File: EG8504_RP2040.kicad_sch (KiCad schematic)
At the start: 52 parts, among them J1 USB_C_Receptacle_USB2.0_16P, J2 522712079, J3 Conn_01x03_Socket, J4 Conn_01x14_Socket, J5 Conn_01x14_Socket, SW1 SW_Push, SW2 SW_Push, U1 RP2040, U2 W25Q16JVSS, U3 MIC5504-3.3YM5, U4 USBLC6-2SC6, U5 MC34063AD, Y1 ECS-3225MV-xxx-xx

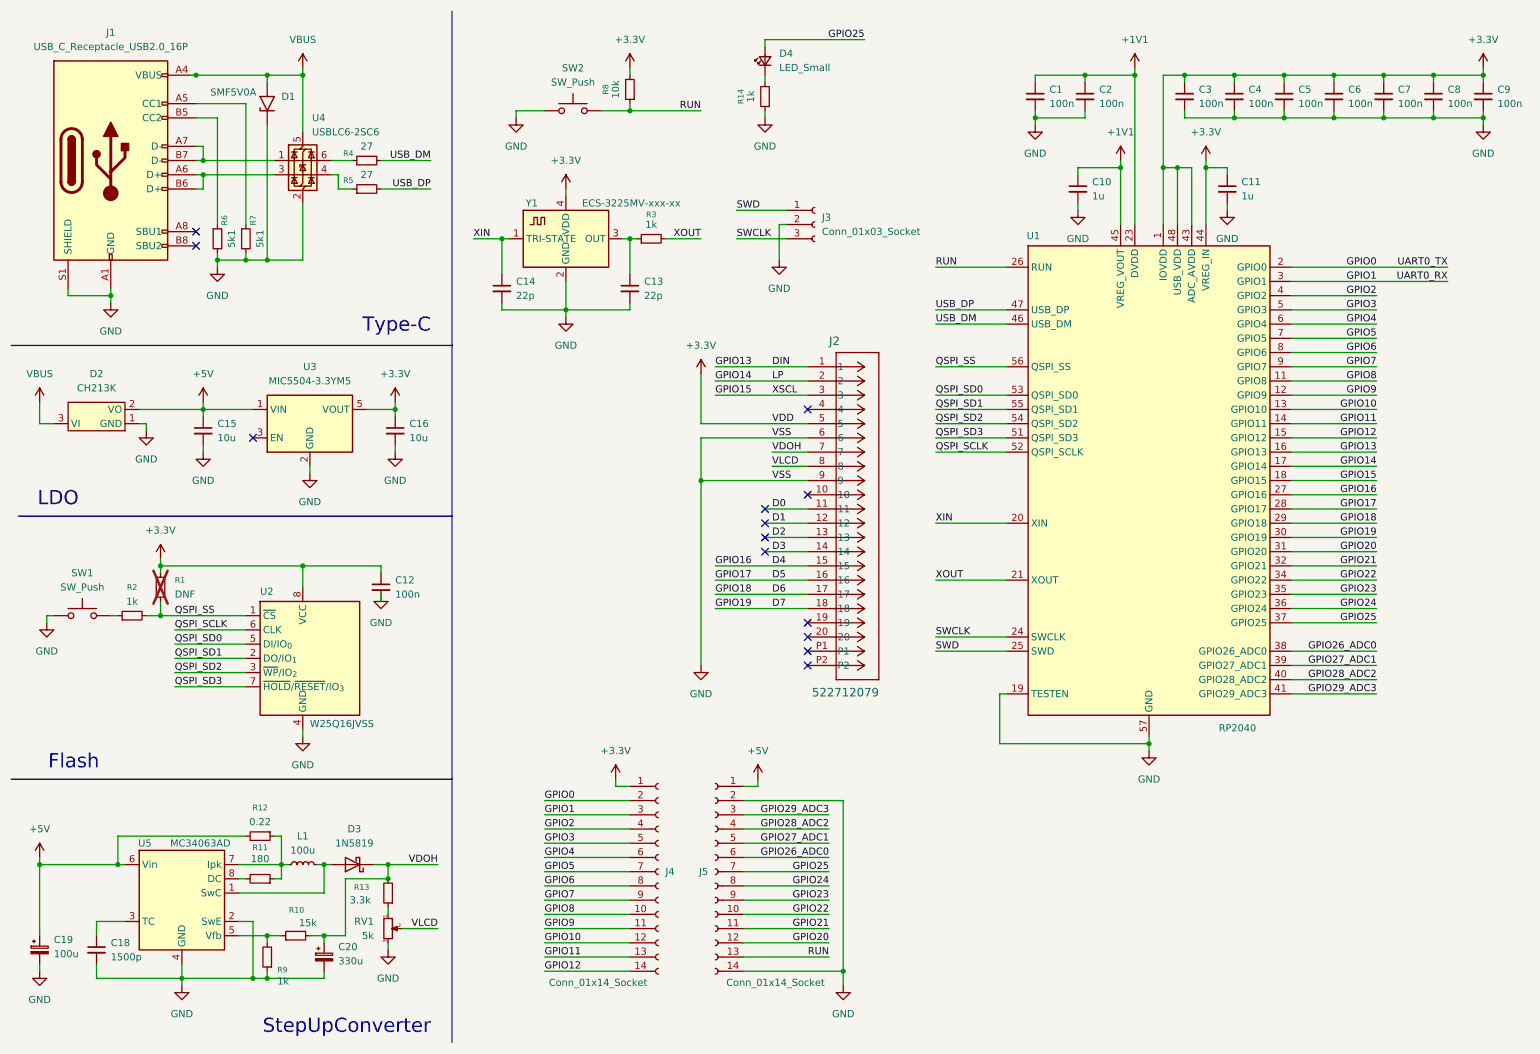
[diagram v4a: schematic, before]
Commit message: rp2040からpicoに変更
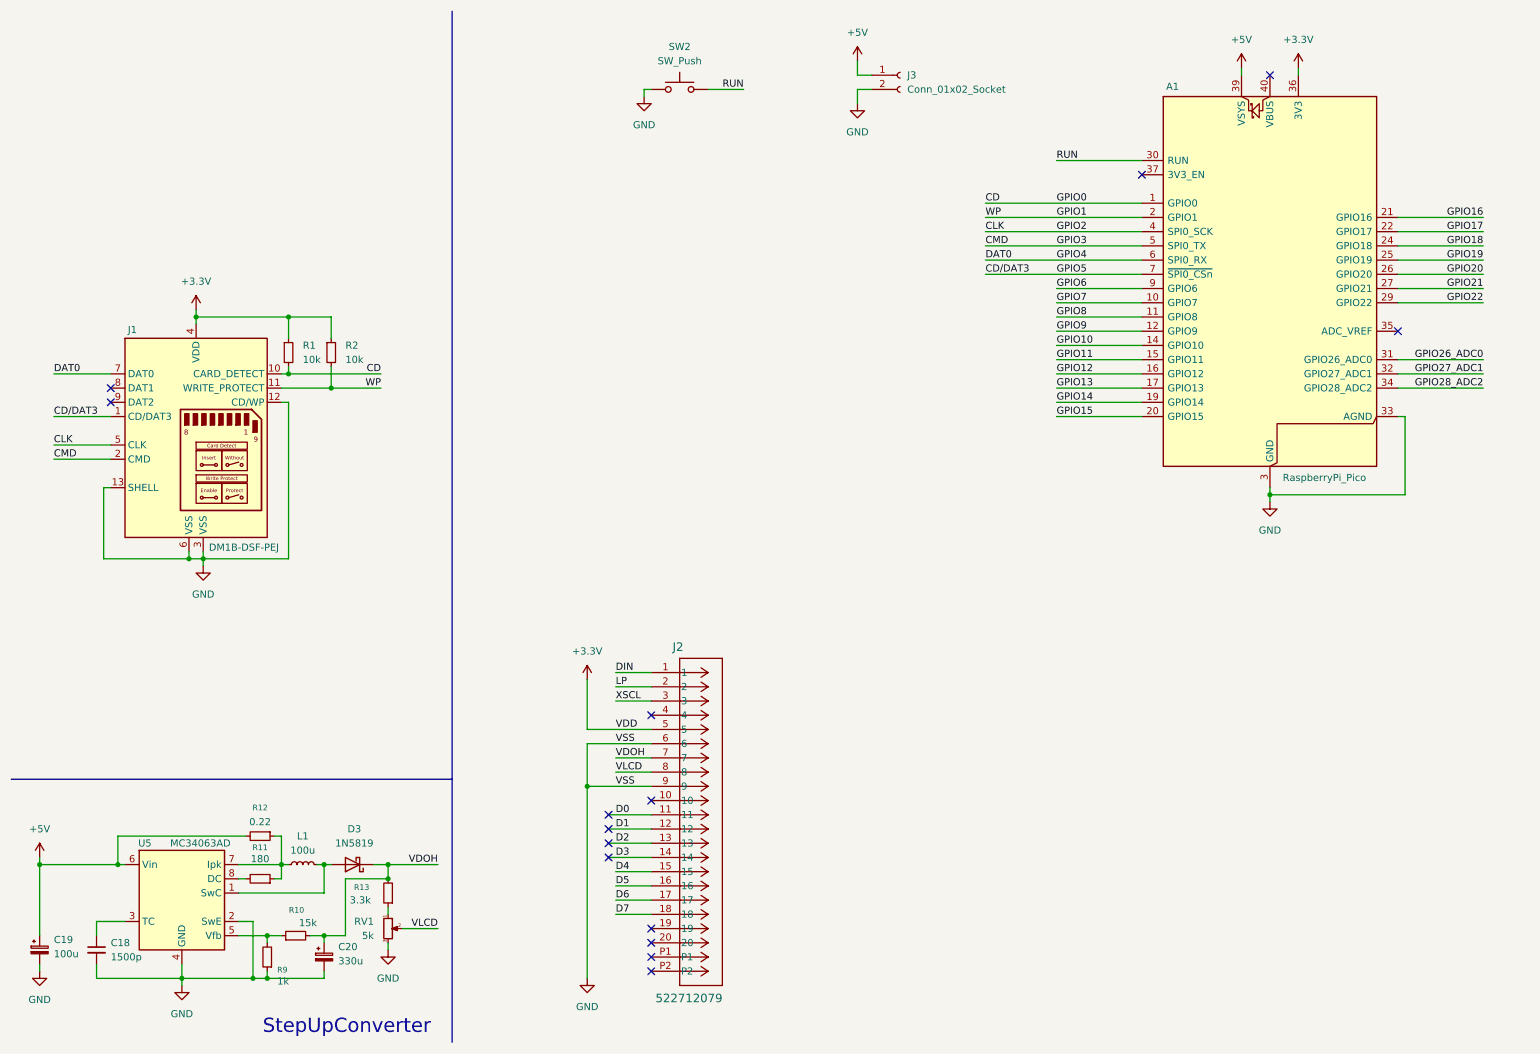
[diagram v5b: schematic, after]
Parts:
- removed C1, C12, C2, C3, C4, C5, C6, C7, C8, C9: 100n, Capacitor_SMD:C_0603_1608Metric_Pad1.08x0.95mm_HandSolder, symbol Device:C_Small
- removed C10, C11: 1u, Capacitor_SMD:C_0603_1608Metric_Pad1.08x0.95mm_HandSolder, symbol Device:C_Small
- removed C13, C14: 22p, Capacitor_SMD:C_0603_1608Metric_Pad1.08x0.95mm_HandSolder, symbol Device:C_Small
- removed C15, C16: 10u, Capacitor_SMD:C_0603_1608Metric_Pad1.08x0.95mm_HandSolder, symbol Device:C_Small
- removed D1: SMF5V0A, Diode_SMD:D_SMF, symbol Diode:SMF5V0A
- removed D2: CH213K, Package_TO_SOT_SMD:SOT-23_Handsoldering, symbol MyLibrary:CH213K
- removed D4: LED_Small, LED_SMD:LED_0603_1608Metric_Pad1.05x0.95mm_HandSolder, symbol Device:LED_Small
- removed J1: USB_C_Receptacle_USB2.0_16P, Connector_USB:USB_C_Receptacle_GCT_USB4105-xx-A_16P_TopMnt_Horizontal, symbol Connector:USB_C_Receptacle_USB2.0_16P
- removed J3: Conn_01x03_Socket, Connector_PinHeader_2.54mm:PinHeader_1x03_P2.54mm_Vertical, symbol Connector:Conn_01x03_Socket
- removed J4, J5: Conn_01x14_Socket, Connector_PinHeader_2.54mm:PinHeader_1x14_P2.54mm_Vertical, symbol Connector:Conn_01x14_Socket
- removed R14, R3: 1k, Resistor_SMD:R_0603_1608Metric_Pad0.98x0.95mm_HandSolder, symbol Device:R_Small
- removed R4, R5: 27, Resistor_SMD:R_0603_1608Metric_Pad0.98x0.95mm_HandSolder, symbol Device:R_Small
- removed R6, R7: 5k1, Resistor_SMD:R_0603_1608Metric_Pad0.98x0.95mm_HandSolder, symbol Device:R_Small
- removed R8: 10k, Resistor_SMD:R_0603_1608Metric_Pad0.98x0.95mm_HandSolder, symbol Device:R_Small
- removed SW1: SW_Push, Button_Switch_SMD:SW_Push_1P1T_NO_Vertical_Wuerth_434133025816, symbol Switch:SW_Push
- removed U1: RP2040, Package_DFN_QFN:QFN-56-1EP_7x7mm_P0.4mm_EP3.2x3.2mm, symbol MCU_RaspberryPi:RP2040
- removed U2: W25Q16JVSS, Package_SO:SOIC-8_5.3x5.3mm_P1.27mm, symbol Memory_Flash:W25Q16JVSS
- removed U3: MIC5504-3.3YM5, Package_TO_SOT_SMD:SOT-23-5, symbol Regulator_Linear:MIC5504-3.3YM5
- removed U4: USBLC6-2SC6, Package_TO_SOT_SMD:SOT-23-6, symbol Power_Protection:USBLC6-2SC6
- removed Y1: ECS-3225MV-xxx-xx, Crystal:Crystal_SMD_3225-4Pin_3.2x2.5mm_HandSoldering, symbol MyLibrary:ECS-3225MV-xxx-xx
- added A1: RaspberryPi_Pico, Module:RaspberryPi_Pico_Common_THT, symbol MCU_Module:RaspberryPi_Pico
- added J1: DM1B-DSF-PEJ, symbol MyLibrary:DM1B-DSF-PEJ
- added J3: Conn_01x02_Socket, symbol Connector:Conn_01x02_Socket
- R1: value DNF -> 10k; footprint Resistor_SMD:R_0603_1608Metric_Pad0.98x0.95mm_HandSolder -> (none); now fitted
- R2: value 1k -> 10k; footprint Resistor_SMD:R_0603_1608Metric_Pad0.98x0.95mm_HandSolder -> (none)
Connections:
- net +3.3V: now also R2.1, A1.36 (3V3), J1.4 (VDD)
- net +5V: now also A1.39 (VSYS), J3.1 (Pin_1)
- net GND: now also A1.13 (GND), A1.18 (GND), A1.23 (GND), A1.28 (GND), A1.3 (GND), A1.33 (AGND), A1.38 (GND), A1.8 (GND), J1.12 (CD/WP), J1.13 (SHELL), J1.3 (VSS), J1.6 (VSS), J3.2 (Pin_2)
- net GPIO1: now also R2.2, A1.2 (GPIO1), J1.11 (WRITE_PROTECT)
- net GPIO10: now also A1.14 (GPIO10)
- net GPIO11: now also A1.15 (GPIO11)
- net GPIO12: now also A1.16 (GPIO12)
- net GPIO14: now also A1.19 (GPIO14); no longer J2.2
- net GPIO15: now also A1.20 (GPIO15); no longer J2.3
- net GPIO20: now also A1.26 (GPIO20)
- net GPIO21: now also A1.27 (GPIO21)
- net GPIO22: now also A1.29 (GPIO22)
- net GPIO26_ADC0: now also A1.31 (GPIO26_ADC0)
- net GPIO27_ADC1: now also A1.32 (GPIO27_ADC1)
- net GPIO28_ADC2: now also A1.34 (GPIO28_ADC2)
- net GPIO6: now also A1.9 (GPIO6)
- net GPIO7: now also A1.10 (GPIO7)
- net GPIO8: now also A1.11 (GPIO8)
- net GPIO9: now also A1.12 (GPIO9)
- net RUN: now also A1.30 (RUN)
- net QSPI_SS renamed CD
- net CD: now also A1.1 (GPIO0), J1.10 (CARD_DETECT); no longer R2.2
- new net CD/DAT3: A1.7 (GPIO5), J1.1 (CD/DAT3)
- new net CLK: A1.4 (GPIO2), J1.5 (CLK)
- new net CMD: A1.5 (GPIO3), J1.2 (CMD)
- new net DAT0: A1.6 (GPIO4), J1.7 (DAT0)
- new net GPIO13: A1.17 (GPIO13)
- new net GPIO16: A1.21 (GPIO16)
- new net GPIO17: A1.22 (GPIO17)
- new net GPIO18: A1.24 (GPIO18)
- new net GPIO19: A1.25 (GPIO19)
- new net LP: J2.2
- new net XSCL: J2.3
- no-connect marks 13 -> 15
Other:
- note removed: "Flash"
- note removed: "LDO"
- note removed: "Type-C"
- moved on the sheet: J2, SW2

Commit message: sd入れたpsb
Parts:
- J1: footprint (none) -> MyLibrary:DM1B-DSF-PEJ
- J3: footprint (none) -> Connector_JST:JST_XH_B2B-XH-A_1x02_P2.50mm_Vertical
- R1, R2: footprint (none) -> Resistor_SMD:R_0603_1608Metric_Pad0.98x0.95mm_HandSolder
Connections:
- net GPIO10 is gone; now on net D5: A1.14 (GPIO10)
- net GPIO11 is gone; now on net D6: A1.15 (GPIO11)
- net GPIO12 is gone; now on net D7: A1.16 (GPIO12)
- net GPIO6 is gone; now on net DIN: A1.9 (GPIO6)
- net GPIO9 is gone; now on net D4: A1.12 (GPIO9)
- net LP is gone; now on net GPIO7: J2.2
- net XSCL is gone; now on net GPIO8: J2.3
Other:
- moved on the sheet: A1, J3, SW2

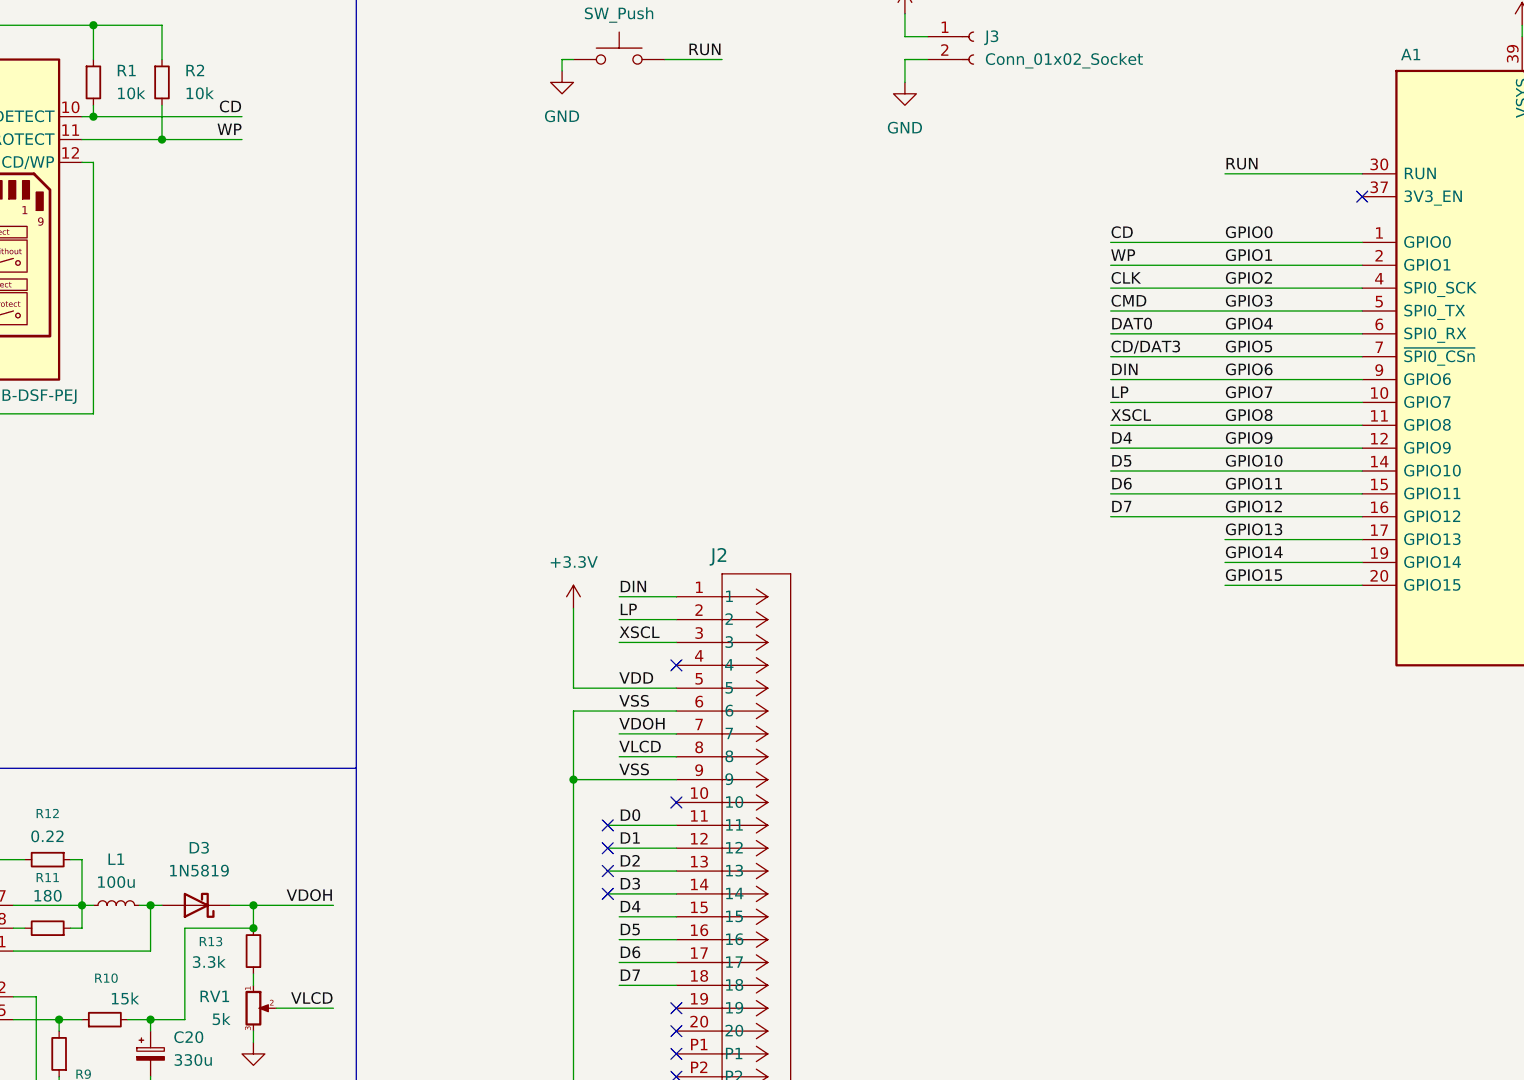
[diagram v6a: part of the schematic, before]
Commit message: sdの向き違った
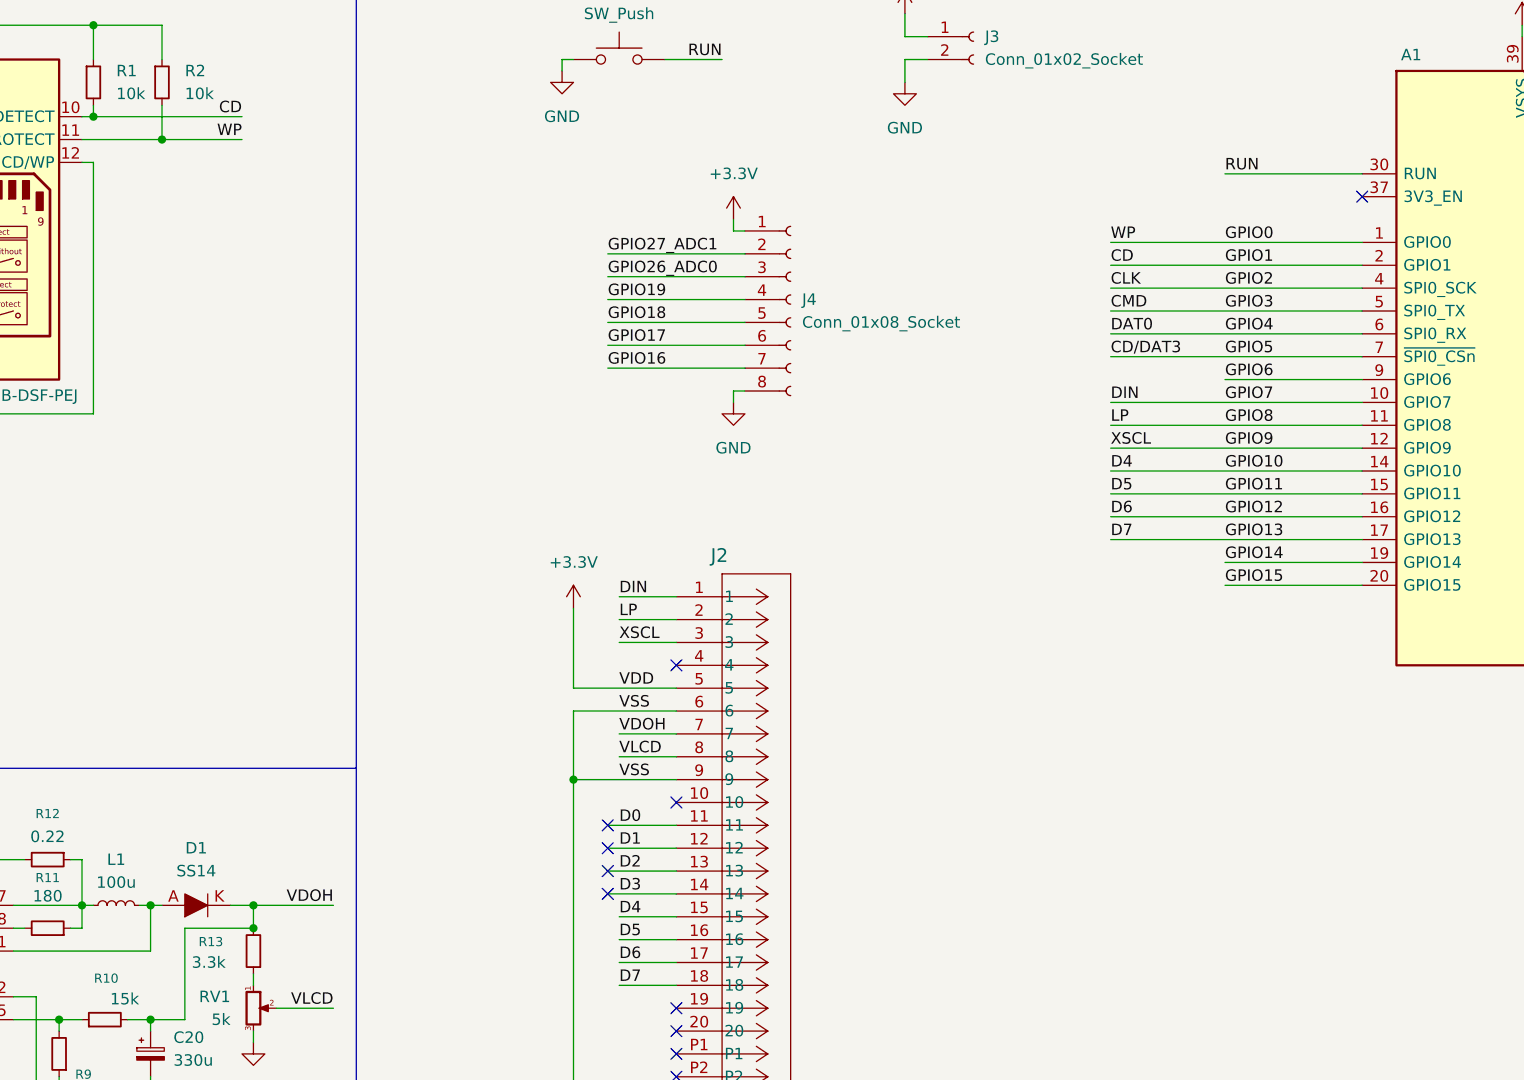
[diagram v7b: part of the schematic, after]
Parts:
- removed D3: 1N5819, Diode_THT:D_DO-41_SOD81_P10.16mm_Horizontal, symbol Diode:1N5819
- added D1: SS14, digikey-footprints:DO-214AC, symbol dk_Diodes-Rectifiers-Single:SS14
- added J4: Conn_01x08_Socket, Connector_JST:JST_XH_B8B-XH-A_1x08_P2.50mm_Vertical, symbol Connector:Conn_01x08_Socket
- L1: footprint (none) -> Inductor_SMD:L_Taiyo-Yuden_NR-10050_9.8x10.0mm_HandSoldering
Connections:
- net GPIO13 is gone; now on net D7: A1.17 (GPIO13)
- net +3.3V: now also J4.1 (Pin_1)
- net CD: now also A1.2 (GPIO1); no longer A1.1 (GPIO0)
- net D4: now also A1.14 (GPIO10); no longer A1.12 (GPIO9)
- net D5: now also A1.15 (GPIO11); no longer A1.14 (GPIO10)
- net D6: now also A1.16 (GPIO12); no longer A1.15 (GPIO11)
- net D7: no longer A1.16 (GPIO12)
- net DIN: now also A1.10 (GPIO7); no longer A1.9 (GPIO6)
- net GND: now also J4.8 (Pin_8)
- net GPIO16: now also J4.7 (Pin_7)
- net GPIO17: now also J4.6 (Pin_6)
- net GPIO18: now also J4.5 (Pin_5)
- net GPIO19: now also J4.4 (Pin_4)
- net GPIO26_ADC0: now also J4.3 (Pin_3)
- net GPIO27_ADC1: now also J4.2 (Pin_2)
- net GPIO8: now also J2.2; no longer J2.3
- net VDOH: now also D1.K
- net at L1.2, U5.1 (SwC): now also D1.A
- net GPIO1 renamed GPIO0
- net GPIO0: now also A1.1 (GPIO0); no longer A1.2 (GPIO1)
- removed net GPIO7: A1.10 (GPIO7), J2.2
- new net GPIO6: A1.9 (GPIO6)
- new net GPIO9: A1.12 (GPIO9), J2.3

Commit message: DHT11を追加
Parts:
- added J5: Conn_01x04_Socket, Connector_JST:JST_XH_B4B-XH-A_1x04_P2.50mm_Vertical, symbol Connector:Conn_01x04_Socket
- added JP1: SolderJumper_2_Open, Jumper:SolderJumper-2_P1.3mm_Open_RoundedPad1.0x1.5mm, symbol Jumper:SolderJumper_2_Open
- added R3: 10k, Resistor_SMD:R_0603_1608Metric_Pad0.98x0.95mm_HandSolder, symbol Device:R_Small
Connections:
- net +3.3V: now also J5.1 (Pin_1), R3.2
- net GND: now also J5.4 (Pin_4), JP1.2 (B)
- net GPIO15: now also J5.2 (Pin_2), R3.1
- new net: J5.3 (Pin_3), JP1.1 (A)
